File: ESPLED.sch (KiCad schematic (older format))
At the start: 43 parts, among them CON1 BARREL_JACK, J1 USB_B_Micro, J2 LED_CON_RGB, J3 LED_CON_WW, J4 MIC, P1 LED_CON_SCREW, P2 LED_CON_SCREW, P3 LED_CON_SCREW, Q1 IRLZ34N, Q2 IRLZ34N, Q3 IRLZ34N, Q4 IRLZ34N, Q5 IRLZ34N, SW1 Reset, SW2 Program, SW3 Mode, U1 AMS1117-3.3, U2 ESP-07v2, U3 INTERFACE-CH340G, U4 DS18B20, Y1 Crystal

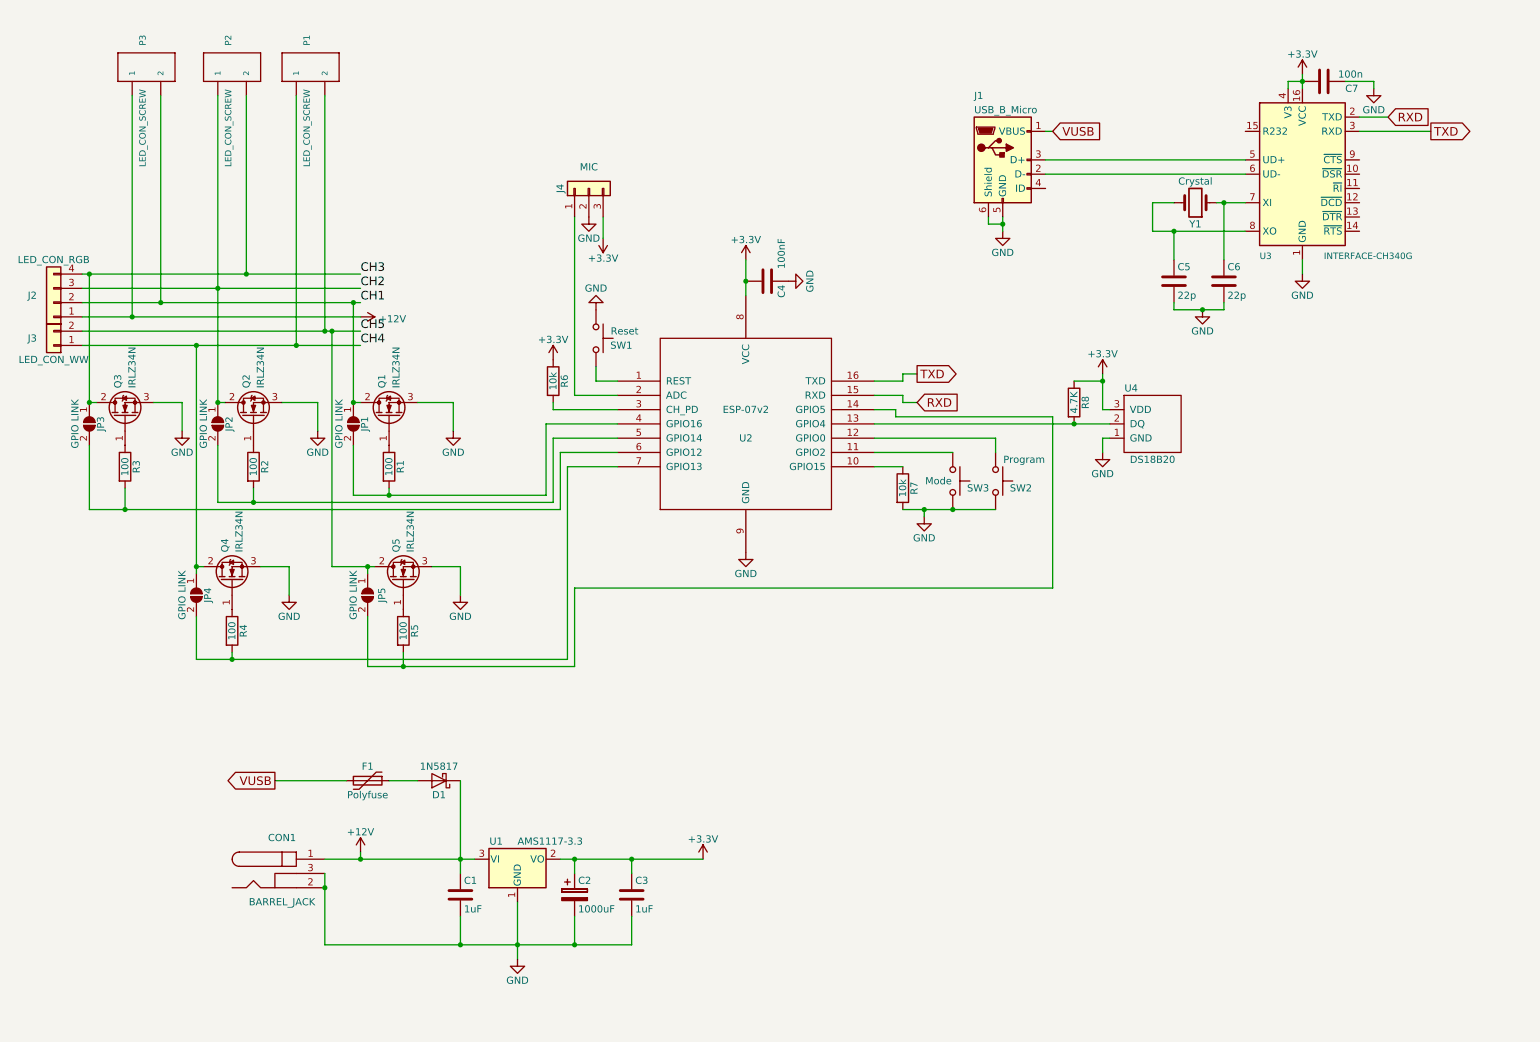
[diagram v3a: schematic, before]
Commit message: Logic Level Converter added. Schematic finished
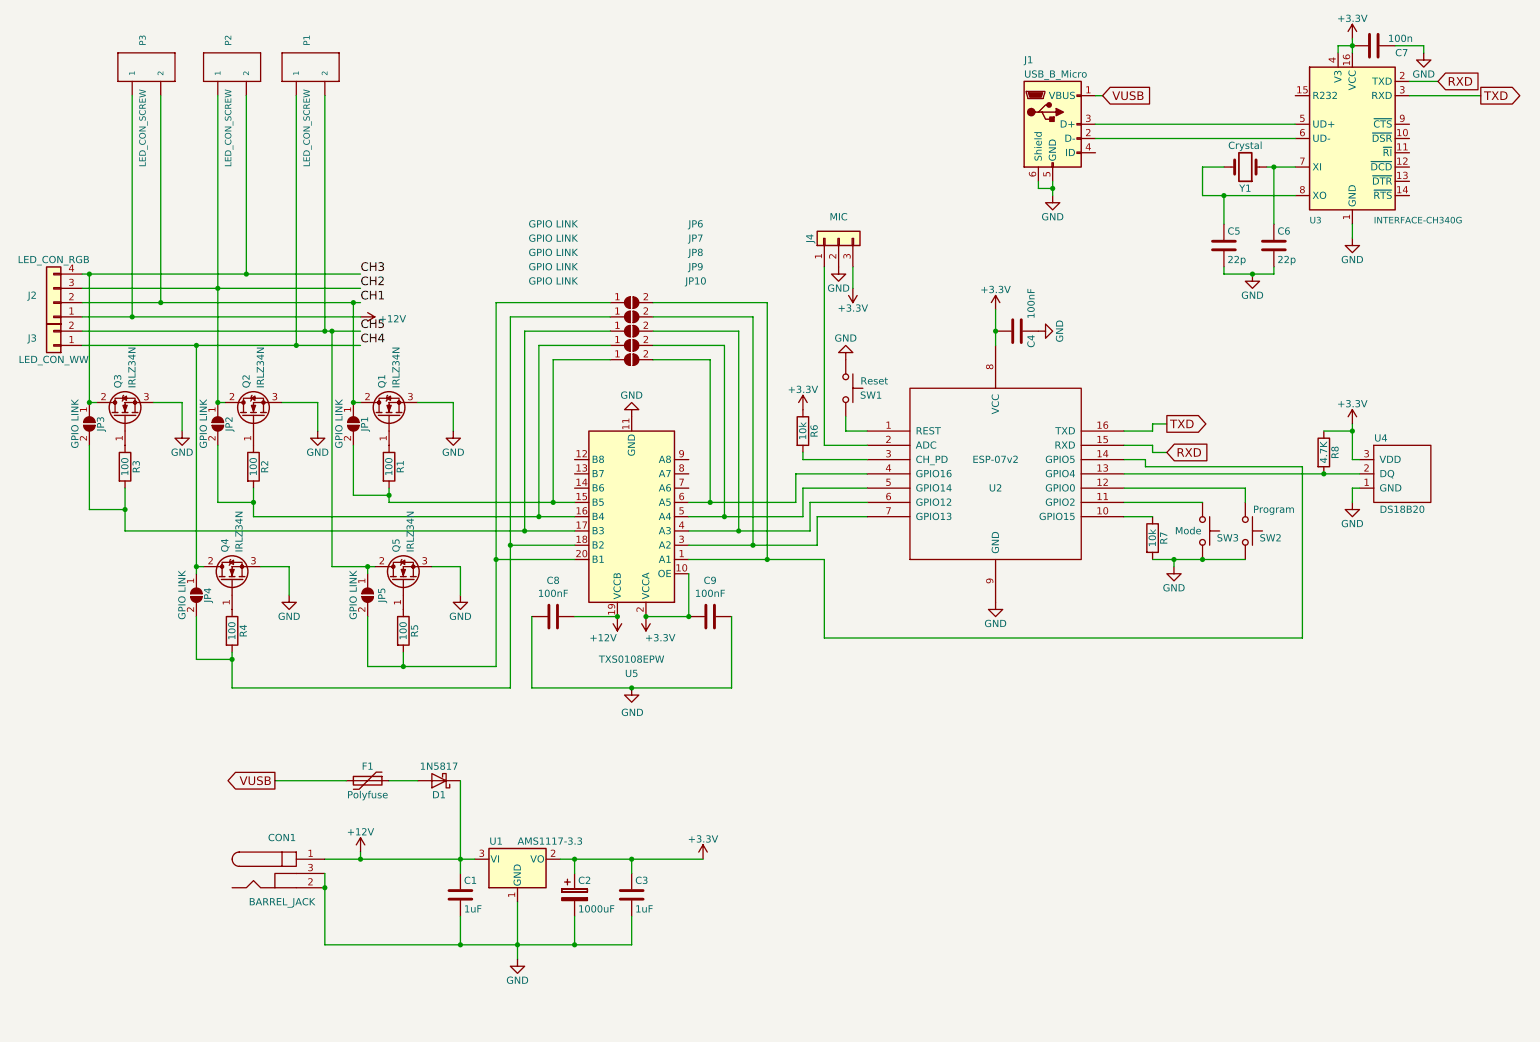
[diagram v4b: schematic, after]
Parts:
- added C8, C9: 100nF, Capacitor_SMD:C_0603_1608Metric_Pad1.05x0.95mm_HandSolder, symbol Device:C
- added JP10, JP6, JP7, JP8, JP9: GPIO LINK, Jumper:SolderJumper-2_P1.3mm_Open_RoundedPad1.0x1.5mm, symbol Jumper:SolderJumper_2_Open
- added U5: TXS0108EPW, Package_SO:TSSOP-20_4.4x6.5mm_P0.65mm, symbol Logic_LevelTranslator:TXS0108EPW
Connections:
- net +12V: now also C8.1, U5.19 (VCCB)
- net +3V3: now also C9.2, U5.10 (OE), U5.2 (VCCA)
- net GND: now also C8.2, C9.1, U5.11 (GND)
- net at JP5.2 (B), R5.2: now also JP6.1 (A), U5.20 (B1); no longer U2.14 (GPIO5)
- net at JP1.2 (B), R1.2: now also JP10.1 (A), U5.15 (B5); no longer U2.4 (GPIO16)
- net at JP2.2 (B), R2.2: now also JP9.1 (A), U5.16 (B4); no longer U2.5 (GPIO14)
- net at JP3.2 (B), R3.2: now also JP8.1 (A), U5.17 (B3); no longer U2.6 (GPIO12)
- net at JP4.2 (B), R4.2: now also JP7.1 (A), U5.18 (B2); no longer U2.7 (GPIO13)
- new net: JP6.2 (B), U2.14 (GPIO5), U5.1 (A1)
- new net: JP10.2 (B), U2.4 (GPIO16), U5.6 (A5)
- new net: JP9.2 (B), U2.5 (GPIO14), U5.5 (A4)
- new net: JP8.2 (B), U2.6 (GPIO12), U5.4 (A3)
- new net: JP7.2 (B), U2.7 (GPIO13), U5.3 (A2)
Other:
- moved on the sheet: C4, C5, C6, C7, J1, J4, R6, R7, R8, SW1, SW2, SW3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

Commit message: Routed
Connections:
- net SIG1: now reaches JP6.2 (B), U2.14 (GPIO5)
- net SIG1: now also U5.3 (A2); no longer U5.1 (A1)
- net SIG3: now reaches U2.5 (GPIO14), U5.5 (A4)
- net SIG3: now also JP8.2 (B); no longer JP9.2 (B)
- net HSIG1: now reaches JP1.2 (B), R1.2
- net HSIG1: now also JP6.1 (A), U5.18 (B2); no longer JP10.1 (A), U5.15 (B5)
- net HSIG2: now reaches JP2.2 (B), R2.2
- net HSIG2: now also JP7.1 (A), U5.17 (B3); no longer JP9.1 (A), U5.16 (B4)
- net HSIG3: now reaches JP3.2 (B), JP8.1 (A), R3.2
- net HSIG3: now also U5.16 (B4); no longer U5.17 (B3)
- net HSIG4: now reaches JP4.2 (B), R4.2
- net HSIG4: now also JP9.1 (A), U5.15 (B5); no longer JP7.1 (A), U5.18 (B2)
- net HSIG5: now reaches JP5.2 (B), R5.2
- net HSIG5: now also JP10.1 (A), U5.14 (B6); no longer JP6.1 (A), U5.20 (B1)
- net SIG5: now reaches U5.7 (A6)
- net SIG5: now also JP10.2 (B), U2.7 (GPIO13)
- new net SIG2: JP7.2 (B), U2.4 (GPIO16), U5.4 (A3)
- new net SIG4: JP9.2 (B), U2.6 (GPIO12), U5.6 (A5)
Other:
- moved on the sheet: C1, C2, C3, C4, C5, C6, C7, C8, C9, CON1, D1, F1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
